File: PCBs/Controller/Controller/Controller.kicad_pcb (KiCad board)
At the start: 2 copper layers, 91.4 x 77.5 mm, 48 parts, among them J1 Conn_01x06_Male, J2 BATT_01x02_Male, SW1 SW_Push_Dual, SW2 SW_Push_Dual, SW3 SW_SPDT, SW4 SW_SPDT, U1 LF50_TO220, U2 LF33_TO220, U24L1 NRF24L01_Breakout, U24L2 NRF24L01_Breakout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

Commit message: Reduced complexity, removed 1 rf module
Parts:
- removed U24L2: NRF24L01_Breakout, RF_Module:nRF24L01_Breakout
- moved R14 57.4 mm to (148.0, 80.0), turned to 0 degrees
- moved R15 41.3 mm to (193.0, 121.9)
- moved U4 29.8 mm to (149.9, 74.9), turned to 90 degrees
- moved SW2 21.1 mm to (130.8, 77.5)
- moved R5 20.3 mm to (166.4, 102.9), turned to 270 degrees
- moved R2 19.8 mm to (135.9, 59.7)
- moved R4 17.3 mm to (130.8, 59.7)
- moved R6 16.7 mm to (166.4, 100.3)
- moved D5 15.5 mm to (169.5, 102.9)
- moved D2 14.5 mm to (135.9, 66.0)
- moved D4 14.5 mm to (130.8, 66.0)
- moved D6 6.14 mm to (169.5, 98.3)
- moved C5 2.54 mm to (170.2, 94.0)
- moved SW1 2.01 mm to (169.5, 116.8)
- moved C4 1.27 mm to (175.3, 94.0)
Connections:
- SW4 pad 1: RF2 -> Net-(SW4-Pad1)
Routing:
- net D4: track 180.6 -> 68.7 mm
- net 5V: track 110.6 -> 5.98 mm, vias 5 -> 0
- net D8: track 150.3 -> 83.4 mm
- net D13: track 160.3 -> 94.0 mm, vias 2 -> 1
- net D11: track 134.4 -> 73.4 mm
- net D7: track 127.9 -> 74.5 mm
- net D12: track 117.5 -> 64.7 mm
- net RF2: track 52.0 -> 0.00 mm
- net TX: track 98.7 -> 69.9 mm
- net D3: track 68.1 -> 40.6 mm, vias 2 -> 0
- net 3V3: track 108.1 -> 83.2 mm
- net A1: track 9.29 -> 32.0 mm, vias 2 -> 0
- net GND: track 56.0 -> 33.5 mm, vias 12 -> 1
- net A5: track 67.3 -> 48.9 mm, vias 2 -> 0
- net RX: track 84.7 -> 69.7 mm
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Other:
- net class Batt added: clearance 0.4, trace_width 0.5, via_dia 1.2, via_drill 0.4

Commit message: Generating Gerber Files for 2.0 board rev (Sent for manufacturing)
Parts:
- added G***: LOGO, Logo:WE_logo_5mm, F.Cu at (162.6, 80.6)
- added G***: LOGO, Logo:Hex_inverse, F.Cu at (172.7, 87.6)
- U5, U6: footprint Joystick:JOYSTICK -> Joystick2:JOYSTICK
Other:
- net class Mounting Holes added: clearance 0.2, trace_width 0.25, via_dia 6.5, via_drill 3.9
- board text added: "4DX2 Controller Rev 1.2"
- board text added: "Board made by Will Ehman"

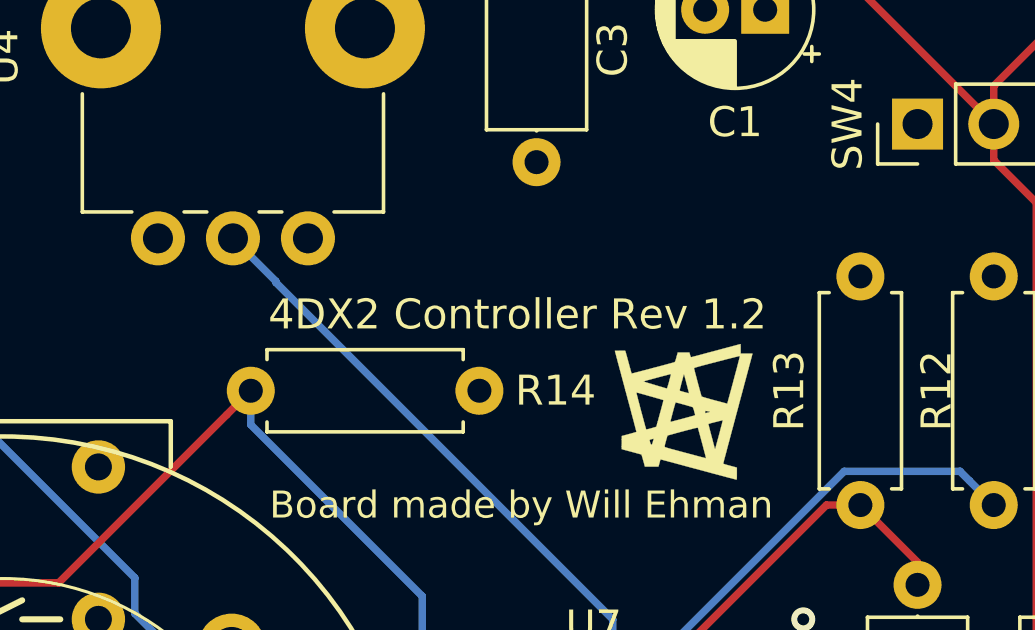
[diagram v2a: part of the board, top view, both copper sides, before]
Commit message: Developed Receiver Schematic and PCB for 1.0
Identified issue with Controller programming header VCC not properly connected to 5V - Can be fixed with jumper in production - rev 1.3 made
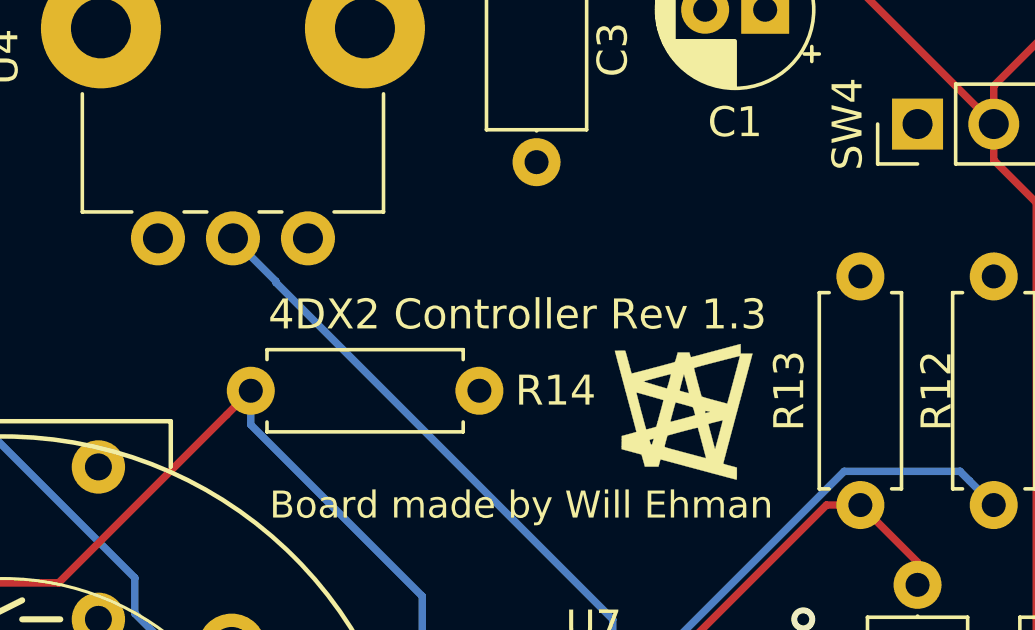
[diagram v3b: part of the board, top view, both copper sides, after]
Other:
- board text added: "4DX2 Controller Rev 1.3"
- board text removed: "4DX2 Controller Rev 1.2"
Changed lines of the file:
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@@
   )
   (gr_arc (start 215.9 123.19) (end 215.9 125.73) (angle -90) (layer Edge.Cuts) (width 0.15))
-  (gr_text "4DX2 Controller Rev 1.2" (at 156.845 77.47) (layer F.SilkS)
+  (gr_text "4DX2 Controller Rev 1.3" (at 156.845 77.47) (layer F.SilkS)
     (effects (font (size 1 1) (thickness 0.2)))
   )
